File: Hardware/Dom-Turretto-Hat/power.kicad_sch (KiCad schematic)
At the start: 28 parts, among them J3 Barrel_Jack_Switch, J4 Conn_01x02, Q1 RSJ250P10TL, Q2 RSJ250P10TL, U2 LTC4412xS6, U3 LM22679TJ-5.0{slash}NOPB, U6 LT1963AxST-3.3, U7 LTC4411ES5TRMPBF

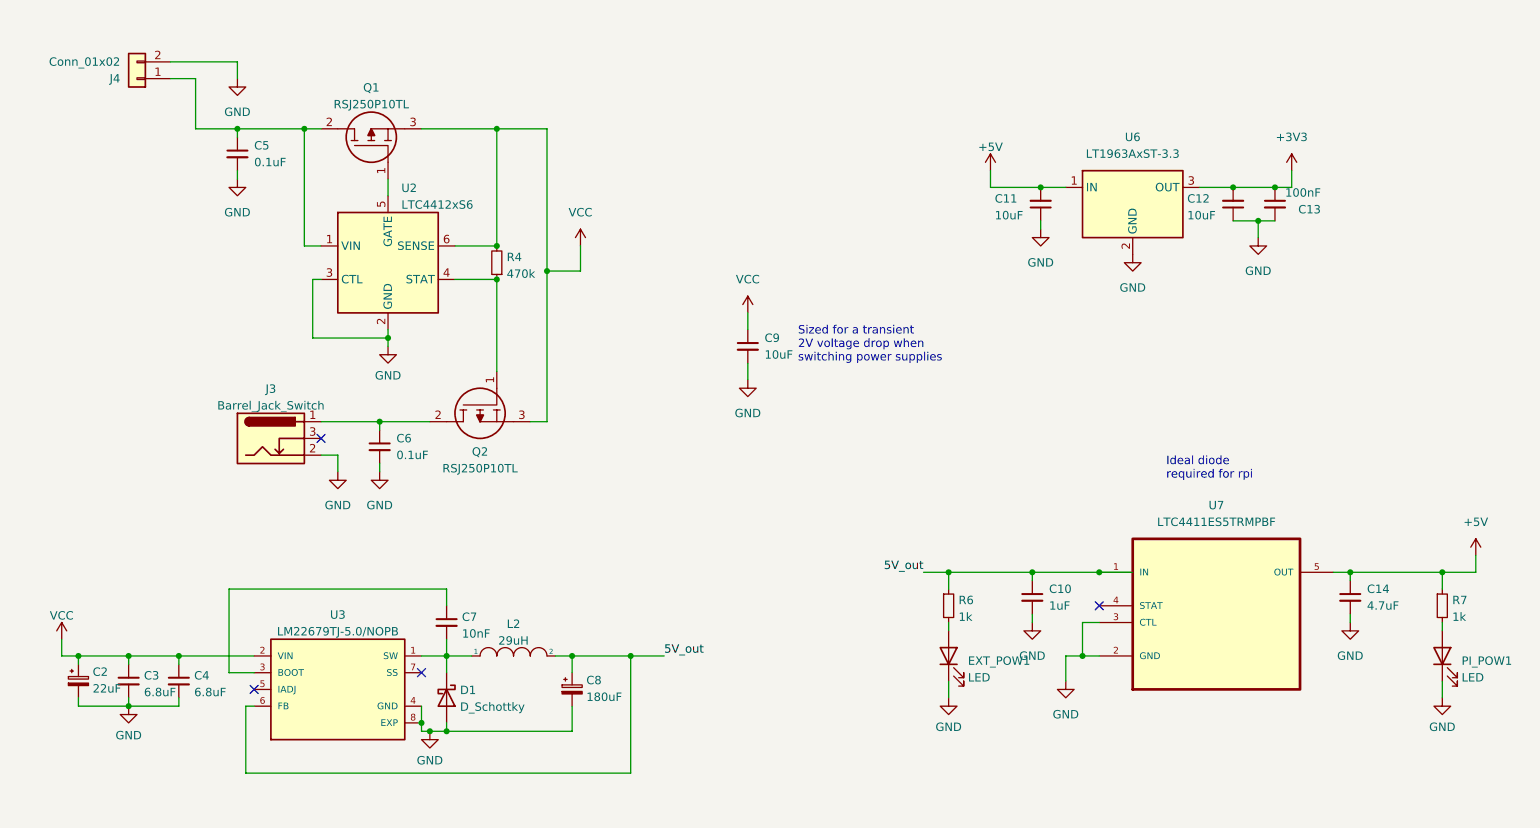
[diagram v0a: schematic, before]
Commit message: Fix power circuitry values
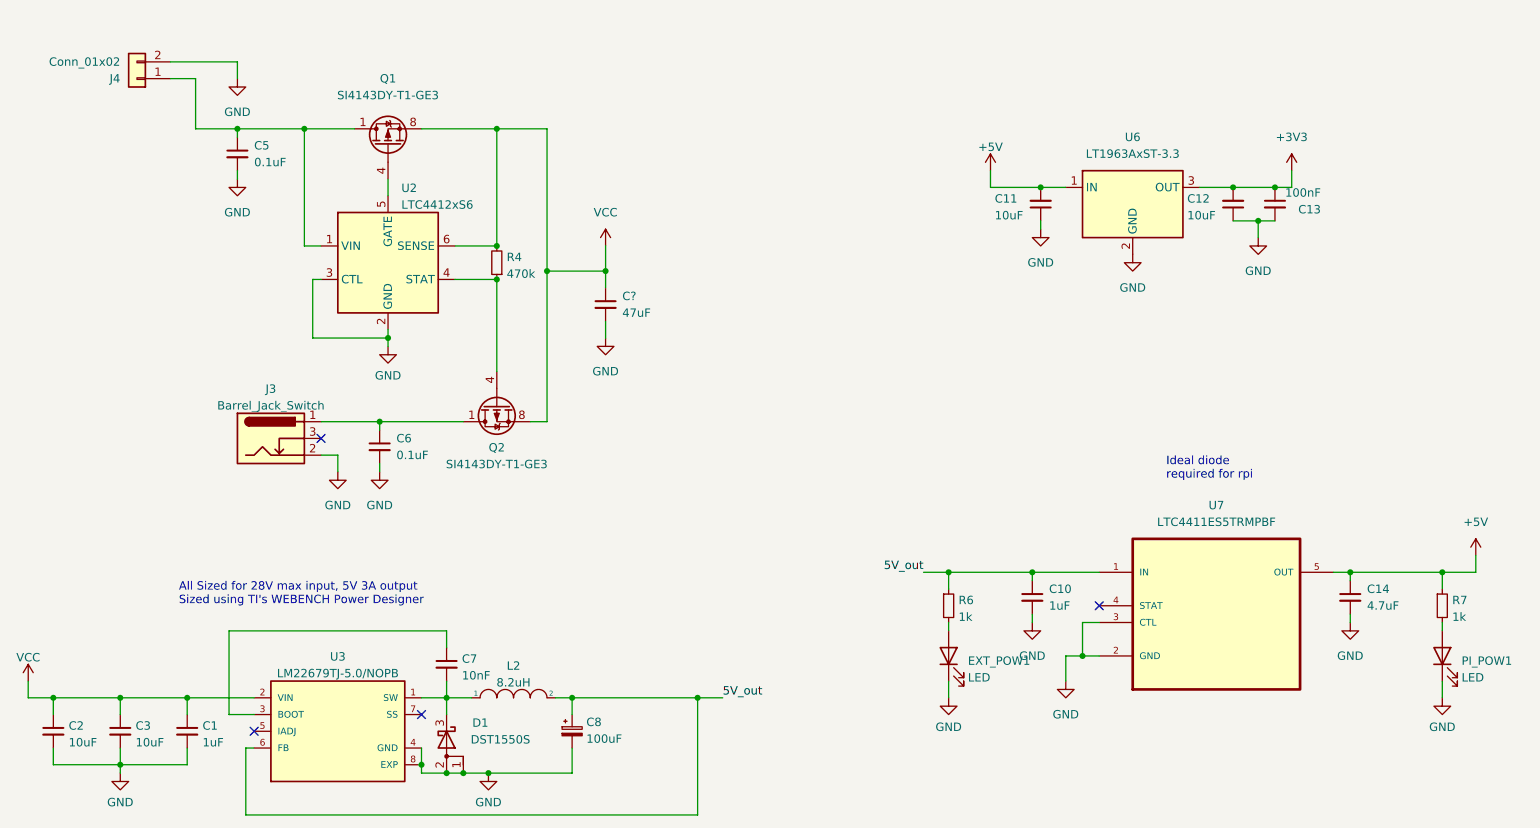
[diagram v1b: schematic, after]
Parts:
- removed C2: 22uF, Capacitor_SMD:C_0603_1608Metric, symbol Device:C_Polarized_Small
- removed C4: 6.8uF, Capacitor_SMD:C_0603_1608Metric, symbol Device:C_Small
- removed C9: 10uF, Capacitor_SMD:C_0603_1608Metric, symbol Device:C_Small
- removed D1: D_Schottky, Diode_SMD:D_SOD-123, symbol Device:D_Schottky
- removed Q1, Q2: RSJ250P10TL, Package_TO_SOT_SMD:TO-263-3_TabPin2, symbol iclr:RSJ250P10TL
- added C1: 1uF, Capacitor_SMD:C_0603_1608Metric, symbol Device:C_Small
- added C2: 10uF, Capacitor_SMD:C_0603_1608Metric, symbol Device:C_Small
- added C?: 47uF, Capacitor_SMD:CP_Elec_6.3x7.7, symbol Device:C_Small
- added D1: DST1550S, Package_TO_SOT_SMD:TO-277B, symbol Device:D_Schottky_AAK
- added Q1, Q2: SI4143DY-T1-GE3, Package_SO:SOIC-8_3.9x4.9mm_P1.27mm, symbol Device:Q_PMOS_GDS
- C3: value 6.8uF -> 10uF
- C8: value 180uF -> 100uF; footprint Capacitor_SMD:CP_Elec_8x11.9 -> Capacitor_SMD:CP_Elec_5x5.9
- L2: value 29uH -> 8.2uH; footprint Inductor_SMD:L_12x12mm_H8mm -> iclr:Bourns_SRP1270
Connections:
- net GND: now also C1.2, C2.2, C?.2, D1.1 (A), D1.2 (A)
- net VCC: now also C1.1, C2.1, C?.1, Q1.5 (D), Q1.6 (D), Q1.7 (D), Q1.8 (D), Q2.5 (D), Q2.6 (D), Q2.7 (D), Q2.8 (D)
- net at C7.2, L2.1, U3.1 (SW): now also D1.3 (K)
- net at C5.1, J4.1 (Pin_1), U2.1 (VIN): now also Q1.1 (S), Q1.2 (S), Q1.3 (S)
- net at R4.1, U2.4 (STAT): now also Q2.4 (G)
- net at U2.5 (GATE): now also Q1.4 (G)
- net at C6.1, J3.1: now also Q2.1 (S), Q2.2 (S), Q2.3 (S)
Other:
- note added: "All Sized for 28V max input, 5V 3A output Sized using TI's WEBENCH Power Designer"
- note removed: "Sized for a transient 2V voltage drop when switching power supplies"
- moved on the sheet: C3, C7, C8, L2, U3

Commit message: Remove 3.3V regulator and use pi power for logic
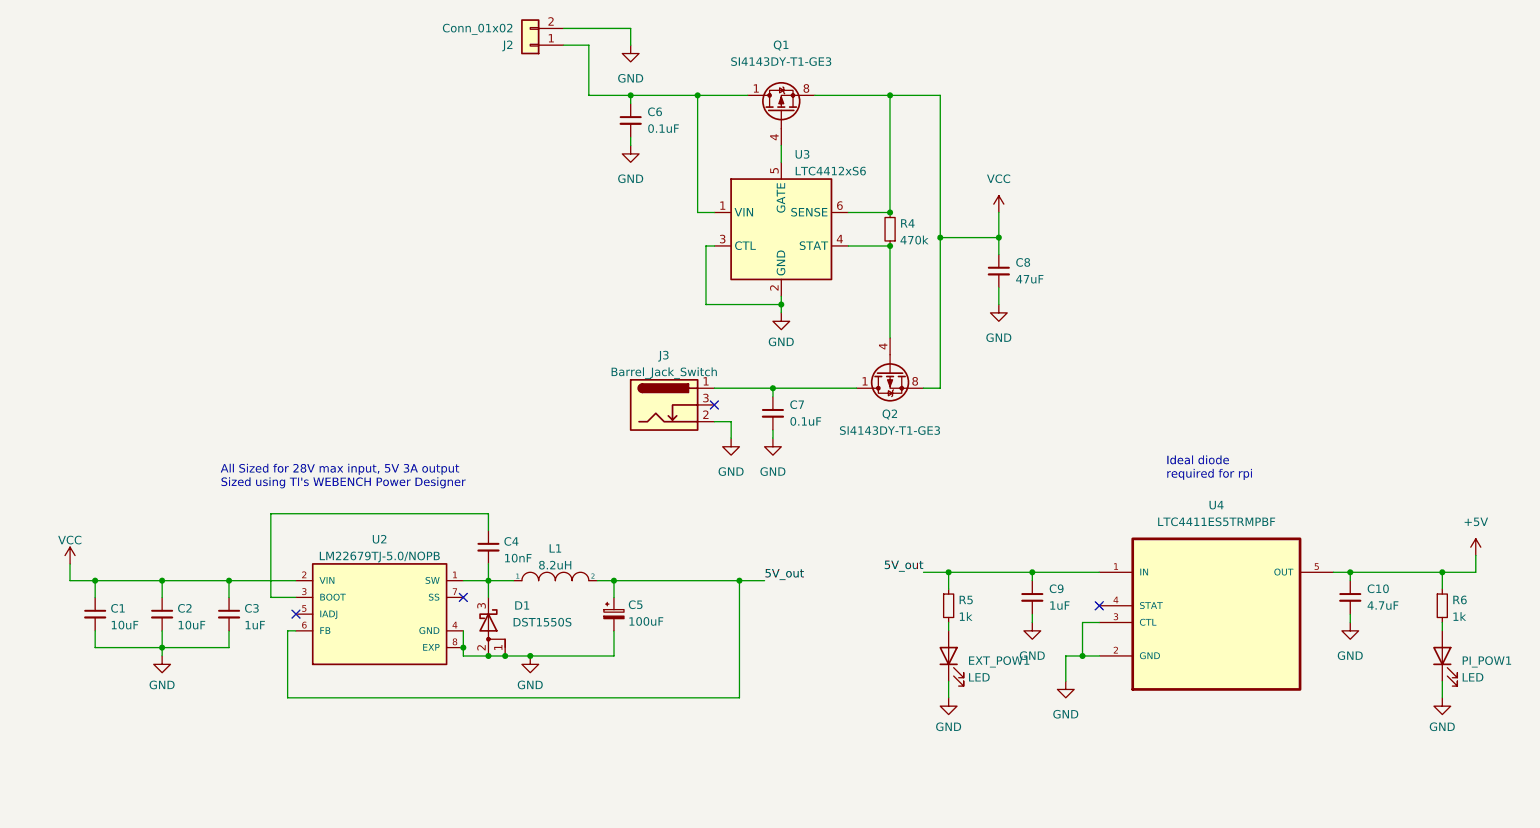
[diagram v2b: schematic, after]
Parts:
- removed C11, C12: 10uF, Capacitor_SMD:C_0603_1608Metric, symbol Device:C_Small
- removed C13: 100nF, Capacitor_SMD:C_0603_1608Metric, symbol Device:C_Small
- removed U6: LT1963AxST-3.3, Package_TO_SOT_SMD:SOT-223-3_TabPin2, symbol Regulator_Linear:LT1963AxST-3.3
- gave numbers to parts that had none: 1
- renumbered C2 to C1, C14 to C10, C3 to C2, C1 to C3, C7 to C4, C8 to C5, C5 to C6, C6 to C7, C10 to C9, J4 to J2, L2 to L1, R6 to R5, R7 to R6, U3 to U2, U2 to U3, U7 to U4
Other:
- moved on the sheet: C1, C2, C3, C4, C5, C6, C7, C8, D1, J2, J3, L1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

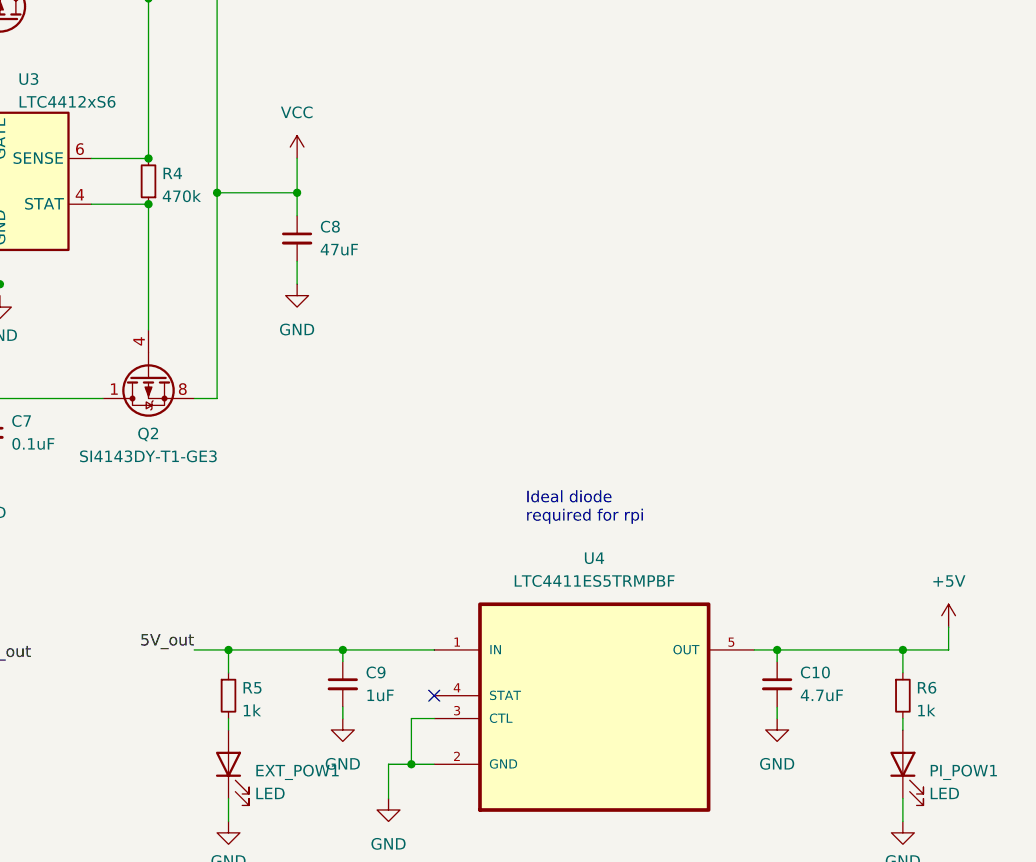
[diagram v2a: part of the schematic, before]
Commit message: Did initial laying out of components
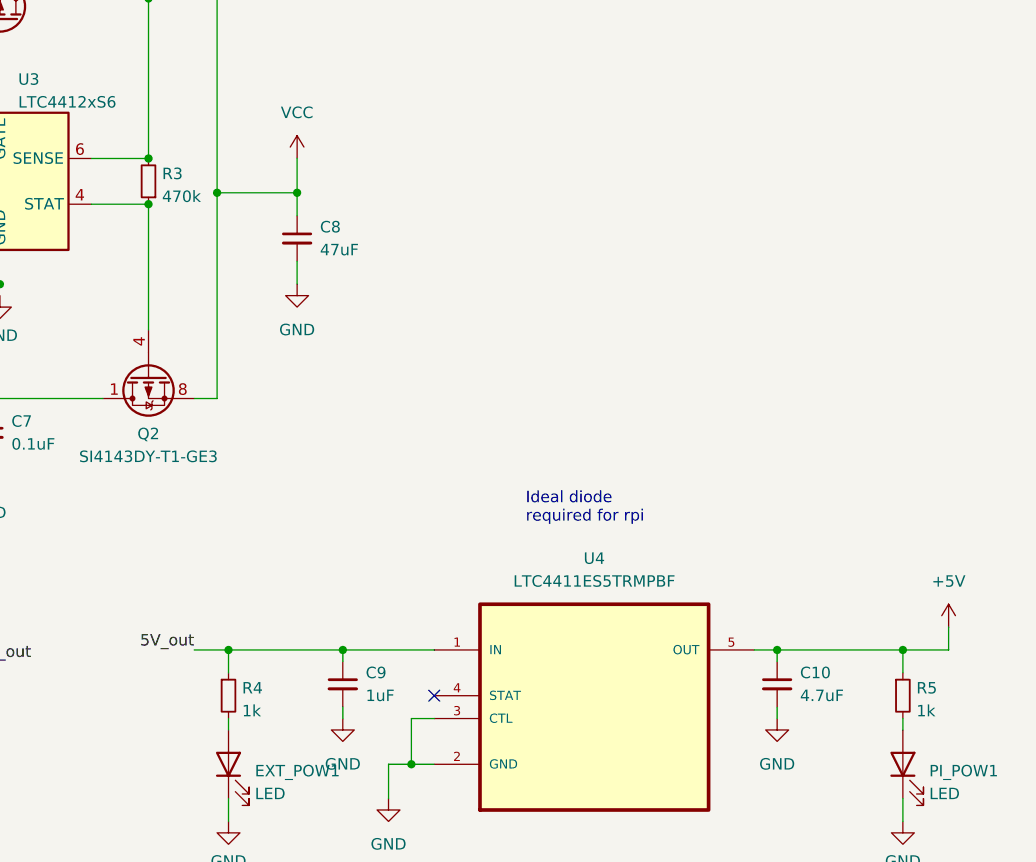
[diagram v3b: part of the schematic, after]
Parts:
- renumbered R4 to R3, R5 to R4, R6 to R5
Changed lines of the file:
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@@
   (symbol (lib_id "power:VCC") (at 182.88 64.77 0) (unit 1)
     (in_bom yes) (on_board yes) (fields_autoplaced)
-    (property "Reference" "#PWR018" (id 0) (at 182.88 68.58 0)
+    (property "Reference" "#PWR019" (id 0) (at 182.88 68.58 0)
       (effects (font (size 1.27 1.27)) hide)
     )
@@
   (symbol (lib_id "power:GND") (at 182.88 78.74 0) (unit 1)
     (in_bom yes) (on_board yes) (fields_autoplaced)
-    (property "Reference" "#PWR019" (id 0) (at 182.88 85.09 0)
+    (property "Reference" "#PWR020" (id 0) (at 182.88 85.09 0)
       (effects (font (size 1.27 1.27)) hide)
     )
@@
   (symbol (lib_id "power:GND") (at 175.26 138.43 0) (unit 1)
     (in_bom yes) (on_board yes) (fields_autoplaced)
-    (property "Reference" "#PWR017" (id 0) (at 175.26 144.78 0)
+    (property "Reference" "#PWR018" (id 0) (at 175.26 144.78 0)
       (effects (font (size 1.27 1.27)) hide)
     )
@@
   (symbol (lib_id "power:GND") (at 142.24 99.06 0) (unit 1)
     (in_bom yes) (on_board yes) (fields_autoplaced)
-    (property "Reference" "#PWR014" (id 0) (at 142.24 105.41 0)
+    (property "Reference" "#PWR015" (id 0) (at 142.24 105.41 0)
       (effects (font (size 1.27 1.27)) hide)
     )
@@
   (symbol (lib_id "power:VCC") (at 41.91 118.11 0) (unit 1)
     (in_bom yes) (on_board yes) (fields_autoplaced)
-    (property "Reference" "#PWR09" (id 0) (at 41.91 121.92 0)
+    (property "Reference" "#PWR010" (id 0) (at 41.91 121.92 0)
       (effects (font (size 1.27 1.27)) hide)
     )
@@
   (symbol (lib_id "power:GND") (at 187.96 127 0) (unit 1)
     (in_bom yes) (on_board yes) (fields_autoplaced)
-    (property "Reference" "#PWR020" (id 0) (at 187.96 133.35 0)
+    (property "Reference" "#PWR021" (id 0) (at 187.96 133.35 0)
       (effects (font (size 1.27 1.27)) hide)
     )
@@
   (symbol (lib_id "power:GND") (at 148.59 99.06 0) (unit 1)
     (in_bom yes) (on_board yes) (fields_autoplaced)
-    (property "Reference" "#PWR015" (id 0) (at 148.59 105.41 0)
+    (property "Reference" "#PWR016" (id 0) (at 148.59 105.41 0)
       (effects (font (size 1.27 1.27)) hide)
     )
@@
   (symbol (lib_id "power:GND") (at 193.04 135.89 0) (unit 1)
     (in_bom yes) (on_board yes) (fields_autoplaced)
-    (property "Reference" "#PWR021" (id 0) (at 193.04 142.24 0)
+    (property "Reference" "#PWR022" (id 0) (at 193.04 142.24 0)
       (effects (font (size 1.27 1.27)) hide)
     )
@@
   (symbol (lib_id "power:GND") (at 149.86 80.01 0) (unit 1)
     (in_bom yes) (on_board yes) (fields_autoplaced)
-    (property "Reference" "#PWR016" (id 0) (at 149.86 86.36 0)
+    (property "Reference" "#PWR017" (id 0) (at 149.86 86.36 0)
       (effects (font (size 1.27 1.27)) hide)
     )
@@
   (symbol (lib_id "power:+5V") (at 255.27 116.84 0) (unit 1)
     (in_bom yes) (on_board yes) (fields_autoplaced)
-    (property "Reference" "#PWR024" (id 0) (at 255.27 120.65 0)
+    (property "Reference" "#PWR025" (id 0) (at 255.27 120.65 0)
       (effects (font (size 1.27 1.27)) hide)
     )
@@
   (symbol (lib_id "Device:R_Small") (at 166.37 67.31 180) (unit 1)
     (in_bom yes) (on_board yes) (fields_autoplaced)
-    (property "Reference" "R4" (id 0) (at 167.8686 66.4753 0)
+    (property "Reference" "R3" (id 0) (at 167.8686 66.4753 0)
       (effects (font (size 1.27 1.27)) (justify right))
     )
@@
   (symbol (lib_id "power:GND") (at 55.88 132.08 0) (unit 1)
     (in_bom yes) (on_board yes) (fields_autoplaced)
-    (property "Reference" "#PWR010" (id 0) (at 55.88 138.43 0)
+    (property "Reference" "#PWR011" (id 0) (at 55.88 138.43 0)
       (effects (font (size 1.27 1.27)) hide)
     )
@@
   (symbol (lib_id "power:GND") (at 127 39.37 0) (unit 1)
     (in_bom yes) (on_board yes) (fields_autoplaced)
-    (property "Reference" "#PWR012" (id 0) (at 127 45.72 0)
+    (property "Reference" "#PWR013" (id 0) (at 127 45.72 0)
       (effects (font (size 1.27 1.27)) hide)
     )
@@
   (symbol (lib_id "power:GND") (at 236.22 127 0) (unit 1)
     (in_bom yes) (on_board yes) (fields_autoplaced)
-    (property "Reference" "#PWR022" (id 0) (at 236.22 133.35 0)
+    (property "Reference" "#PWR023" (id 0) (at 236.22 133.35 0)
       (effects (font (size 1.27 1.27)) hide)
     )
@@
   (symbol (lib_id "power:GND") (at 127 54.61 0) (unit 1)
     (in_bom yes) (on_board yes) (fields_autoplaced)
-    (property "Reference" "#PWR013" (id 0) (at 127 60.96 0)
+    (property "Reference" "#PWR014" (id 0) (at 127 60.96 0)
       (effects (font (size 1.27 1.27)) hide)
     )
@@
   (symbol (lib_id "Device:R_Small") (at 250.19 124.46 0) (unit 1)
     (in_bom yes) (on_board yes) (fields_autoplaced)
-    (property "Reference" "R6" (id 0) (at 251.6886 123.6253 0)
+    (property "Reference" "R5" (id 0) (at 251.6886 123.6253 0)
       (effects (font (size 1.27 1.27)) (justify left))
     )
@@
   (symbol (lib_id "power:GND") (at 111.76 132.08 0) (unit 1)
     (in_bom yes) (on_board yes) (fields_autoplaced)
-    (property "Reference" "#PWR011" (id 0) (at 111.76 138.43 0)
+    (property "Reference" "#PWR012" (id 0) (at 111.76 138.43 0)
       (effects (font (size 1.27 1.27)) hide)
     )
@@
   (symbol (lib_id "power:GND") (at 250.19 138.43 0) (unit 1)
     (in_bom yes) (on_board yes) (fields_autoplaced)
-    (property "Reference" "#PWR023" (id 0) (at 250.19 144.78 0)
+    (property "Reference" "#PWR024" (id 0) (at 250.19 144.78 0)
       (effects (font (size 1.27 1.27)) hide)
     )
@@
   (symbol (lib_id "Device:R_Small") (at 175.26 124.46 0) (unit 1)
     (in_bom yes) (on_board yes) (fields_autoplaced)
-    (property "Reference" "R5" (id 0) (at 176.7586 123.6253 0)
-      (effects (font (size 1.27 1.27)) (justify left))
-    )
+    (property "Reference" "R4" (id 0) (at 176.7586 123.6253 0)
+      (effects (font (size 1.27 1.27)) (justify left))
+    )

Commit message: Made better
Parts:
- added TP7: 5V_Output, TestPoint:TestPoint_Pad_2.0x2.0mm, symbol Connector:TestPoint
- C1, C2: footprint Capacitor_SMD:C_0603_1608Metric -> Capacitor_SMD:C_0805_2012Metric
- C8: value 47uF -> 150uF; footprint Capacitor_SMD:CP_Elec_6.3x7.7 -> Capacitor_SMD:CP_Elec_10x12.5
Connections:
- net 5V_out: now also TP7.1
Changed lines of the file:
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@@
       (effects (font (size 1.27 1.27)) (justify left))
     )
-    (property "Footprint" "Capacitor_SMD:C_0603_1608Metric" (id 2) (at 45.72 125.73 0)
+    (property "Footprint" "Capacitor_SMD:C_0805_2012Metric" (id 2) (at 45.72 125.73 0)
       (effects (font (size 1.27 1.27)) hide)
     )
@@
   (symbol (lib_id "Device:C_Small") (at 182.88 73.66 0) (unit 1)
     (in_bom yes) (on_board yes) (fields_autoplaced)
-    (property "Reference" "C8" (id 0) (at 185.42 72.3962 0)
-      (effects (font (size 1.27 1.27)) (justify left))
-    )
-    (property "Value" "47uF" (id 1) (at 185.42 74.9362 0)
-      (effects (font (size 1.27 1.27)) (justify left))
-    )
-    (property "Footprint" "Capacitor_SMD:CP_Elec_6.3x7.7" (id 2) (at 182.88 73.66 0)
+    (property "Reference" "C8" (id 0) (at 185.2041 72.8316 0)
+      (effects (font (size 1.27 1.27)) (justify left))
+    )
+    (property "Value" "150uF" (id 1) (at 185.2041 75.3685 0)
+      (effects (font (size 1.27 1.27)) (justify left))
+    )
+    (property "Footprint" "Capacitor_SMD:CP_Elec_10x12.5" (id 2) (at 182.88 73.66 0)
       (effects (font (size 1.27 1.27)) hide)
     )
@@
       (effects (font (size 1.27 1.27)) (justify left))
     )
-    (property "Footprint" "Capacitor_SMD:C_0603_1608Metric" (id 2) (at 55.88 125.73 0)
+    (property "Footprint" "Capacitor_SMD:C_0805_2012Metric" (id 2) (at 55.88 125.73 0)
       (effects (font (size 1.27 1.27)) hide)
     )
@@
       (effects (font (size 1.27 1.27)) hide)
     )
+    (pin "1")
+  )
+  (symbol (lib_id "Connector:TestPoint") (at 143.51 120.65 0) (unit 1)
+    (in_bom yes) (on_board yes) (fields_autoplaced)
+    (property "Reference" "TP7" (id 0) (at 144.907 116.5133 0)
+      (effects (font (size 1.27 1.27)) (justify left))
+    )
+    (property "Value" "5V_Output" (id 1) (at 144.907 119.0502 0)
+      (effects (font (size 1.27 1.27)) (justify left))
+    )
+    (property "Footprint" "TestPoint:TestPoint_Pad_2.0x2.0mm" (id 2) (at 148.59 120.65 0)
+      (effects (font (size 1.27 1.27)) hide)
+    )
+    (property "Datasheet" "~" (id 3) (at 148.59 120.65 0)
+      (effects (font (size 1.27 1.27)) hide)
+    )
